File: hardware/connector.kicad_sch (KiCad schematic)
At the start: 3 parts, among them J2 2FA1-NZSP-PCBB6

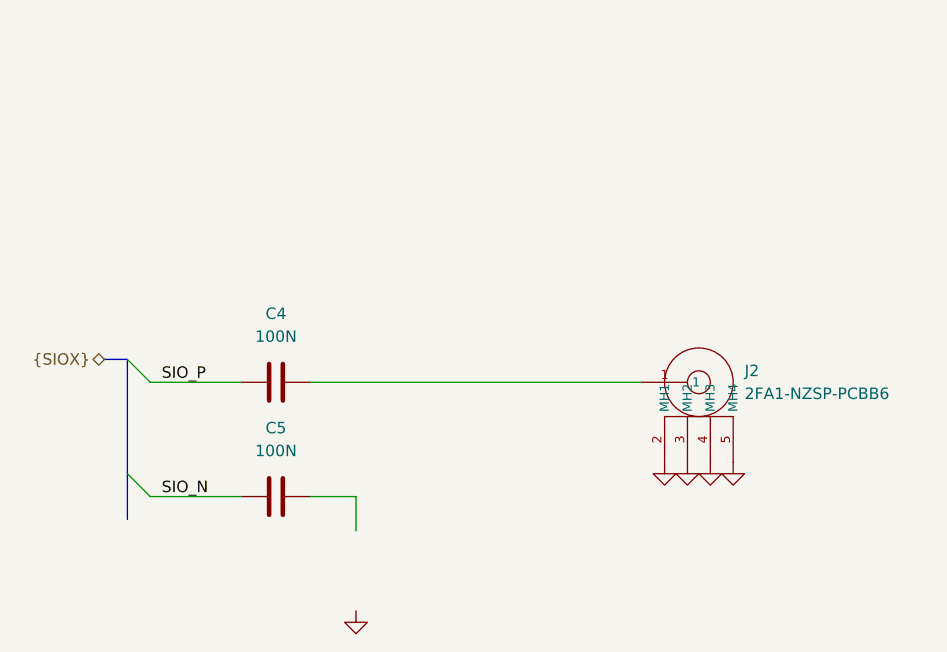
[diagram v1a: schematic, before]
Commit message: cleaned up serializer with comments and project hierarchy
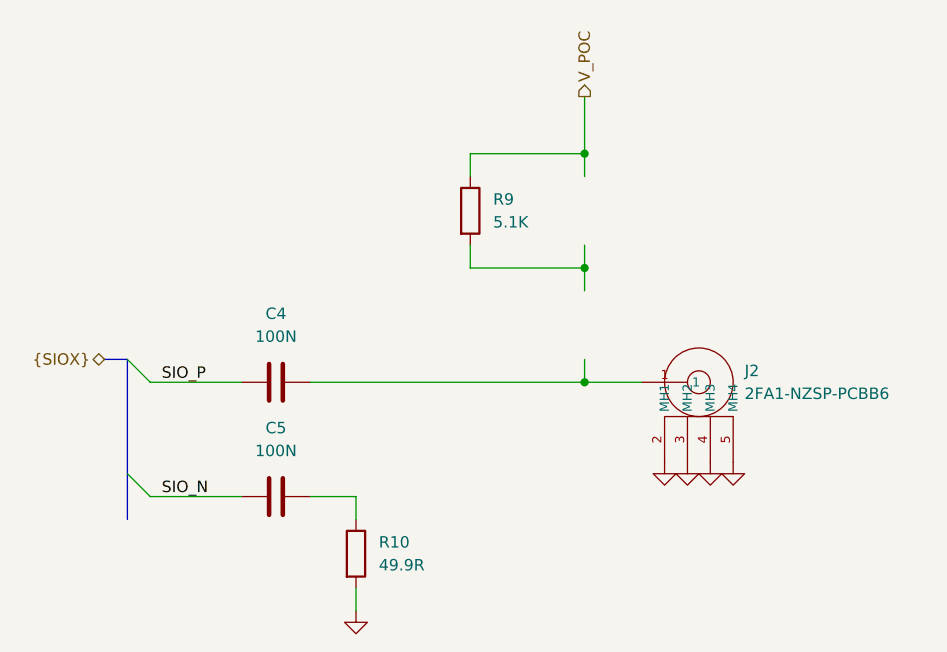
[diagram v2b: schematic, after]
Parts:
- added R10: 49.9R, Resistor_SMD:R_0402_1005Metric, symbol Device:R
- added R9: 5.1K, Resistor_SMD:R_0402_1005Metric, symbol Device:R
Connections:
- net GND: now also R10.2
- net at C5.2: now also R10.1
- new net V_POC: R9.1

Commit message: cleaned up schematics
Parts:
- added L1: PFL1005-561MRW, user:L_Coilcraft_1210POC, symbol user:1210POC-223MRC
- added L2: PFL1005-561MRW, user:L_Coilcraft_PFL1005, symbol user:PFL1005-561MRW
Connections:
- net V_POC: now also L1.1
- net at R9.2: now also L1.2, L2.1
- net at C4.2, J2.1: now also L2.2
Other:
- moved on the sheet: C4, C5, J2, R9

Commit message: started power, added smt fakra
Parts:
- removed J2: 2FA1-NZSP-PCBB6, user:2FA1-NZSP-PCBB6, symbol user:2FA1-NZSP-PCBB6
- added J2: 2FA1-NZSP-PCBB6, user:59S1AC-40MT5-Z, symbol user:59S1AC-40MT5-Z
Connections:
- net GND: now also J2.2 (MH1), J2.3 (MH2), J2.4 (MH3), J2.5 (MH4)
- net at C4.2, L2.2: now also J2.1
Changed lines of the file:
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@@
+	)
+	(symbol
+		(lib_id "user:59S1AC-40MT5-Z")
+		(at 152.4 88.9 0)
+		(unit 1)
+		(exclude_from_sim no)
+		(in_bom yes)
+		(on_board yes)
+		(dnp no)
+		(fields_autoplaced yes)
+		(property "Reference" "J2"
+			(at 157.48 87.6299 0)
+			(effects
+				(font
+					(size 1.27 1.27)
+				)
+				(justify left)
+			)
+		)
+		(property "Value" "2FA1-NZSP-PCBB6"
+			(at 157.48 90.1699 0)
+			(effects
+				(font
+					(size 1.27 1.27)
+				)
+				(justify left)
+			)
+		)
+		(property "Footprint" "user:59S1AC-40MT5-Z"
+			(at 152.4 88.9 0)
+			(effects
+				(font
+					(size 1.27 1.27)
+				)
+				(hide yes)
+			)
+		)
+		(property "Datasheet" ""
+			(at 152.4 88.9 0)
+			(effects
+				(font
+					(size 1.27 1.27)
+				)
+				(hide yes)
+			)
+		)
+		(property "Description" ""
+			(at 152.4 88.9 0)
+			(effects
+				(font
+					(size 1.27 1.27)
+				)
+				(hide yes)
+			)
+		)
+		(pin "4"
+		)
+		(pin "2"
+		)
+		(pin "5"
+		)
+		(pin "1"
+		)
+		(pin "3"
+		)
+		(instances
+			(project ""
+				(path "/d9b03904-3e0d-40cc-bc70-bbd63756773a/877d1132-b95d-4f70-9d75-8a01aff9b6a8"
+					(reference "J2")
+					(unit 1)
+				)
+			)
+		)
 	)
 	(symbol
@@
 					(unit 1)
 				)
-			)
-		)
-	)
-	(symbol
-		(lib_id "user:2FA1-NZSP-PCBB6")
-		(at 152.4 88.9 0)
-		(unit 1)
-		(exclude_from_sim no)
-		(in_bom yes)
-		(on_board yes)
-		(dnp no)
-		(fields_autoplaced yes)
-		(property "Reference" "J2"
-			(at 157.48 87.6299 0)
-			(effects
-				(font
-					(size 1.27 1.27)
-				)
-				(justify left)
-			)
-		)
-		(property "Value" "2FA1-NZSP-PCBB6"
-			(at 157.48 90.1699 0)
-			(effects
-				(font
-					(size 1.27 1.27)
-				)
-				(justify left)
-			)
-		)
-		(property "Footprint" "user:2FA1-NZSP-PCBB6"
-			(at 152.4 88.9 0)
-			(effects
-				(font
-					(size 1.27 1.27)
-				)
-				(hide yes)
-			)
-		)
-		(property "Datasheet" ""
-			(at 152.4 88.9 0)
-			(effects
-				(font
-					(size 1.27 1.27)
-				)
-				(hide yes)
-			)
-		)
-		(property "Description" ""
-			(at 152.4 88.9 0)
-			(effects
-				(font
-					(size 1.27 1.27)
-				)
-				(hide yes)
-			)
-		)
-		(pin "1"
-		)
-		(pin "3"
-		)
-		(pin "5"
-		)
-		(pin "2"
-		)
-		(pin "4"
-		)
-		(instances
-			(project "minimax"
-				(path "/d9b03904-3e0d-40cc-bc70-bbd63756773a/877d1132-b95d-4f70-9d75-8a01aff9b6a8"
-					(reference "J2")
-					(unit 1)
-				)

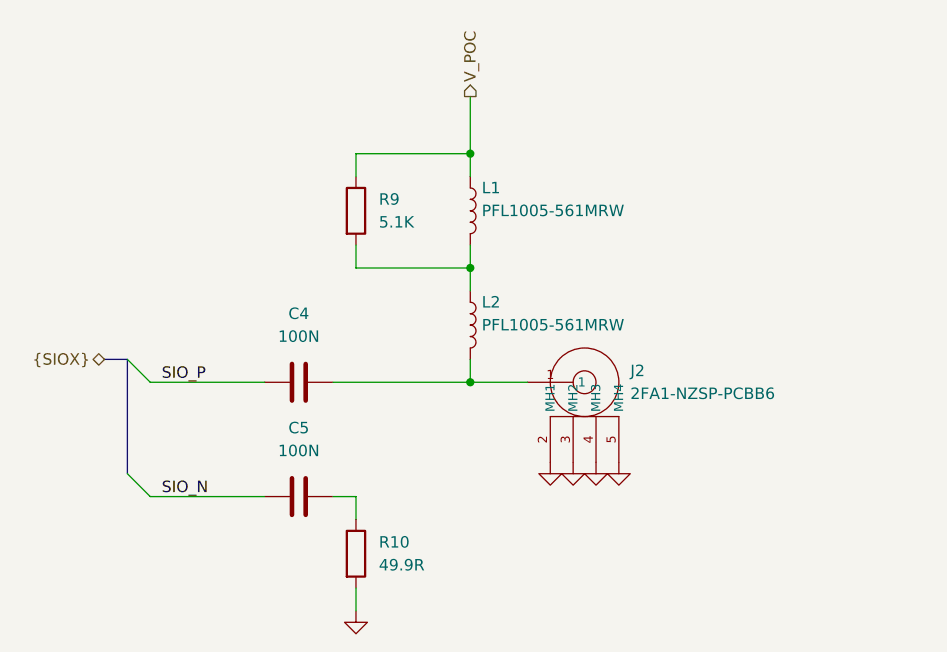
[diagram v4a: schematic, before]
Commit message: finished schematic, changed to 4 layer board
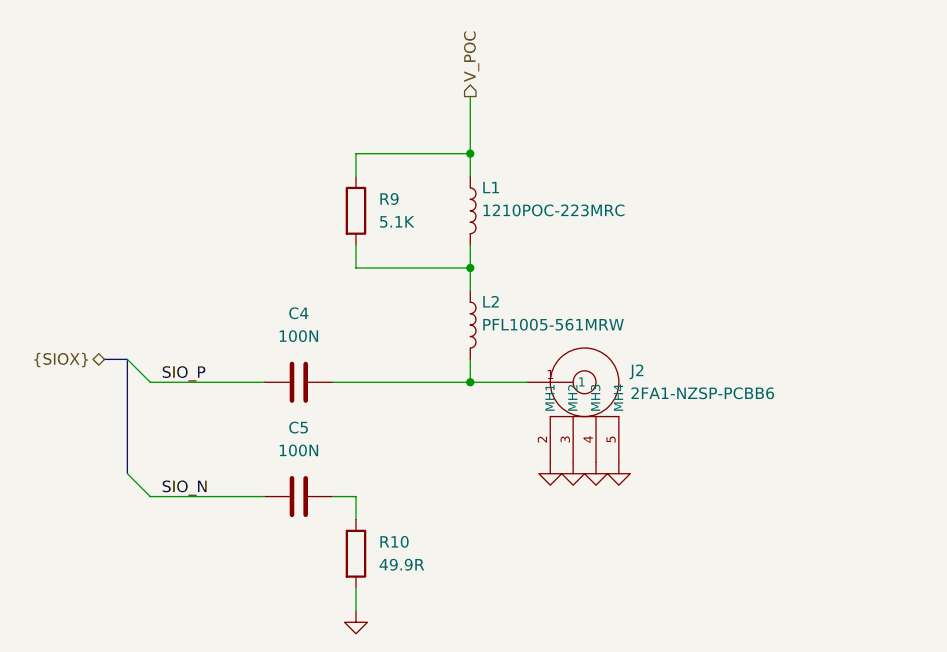
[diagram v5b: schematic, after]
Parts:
- L1: value PFL1005-561MRW -> 1210POC-223MRC
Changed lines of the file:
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@@
 			)
 		)
-		(property "Value" "PFL1005-561MRW"
+		(property "Value" "1210POC-223MRC"
 			(at 140.97 69.8499 0)
 			(effects

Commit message: layout planning and decided to use bottom layer for components
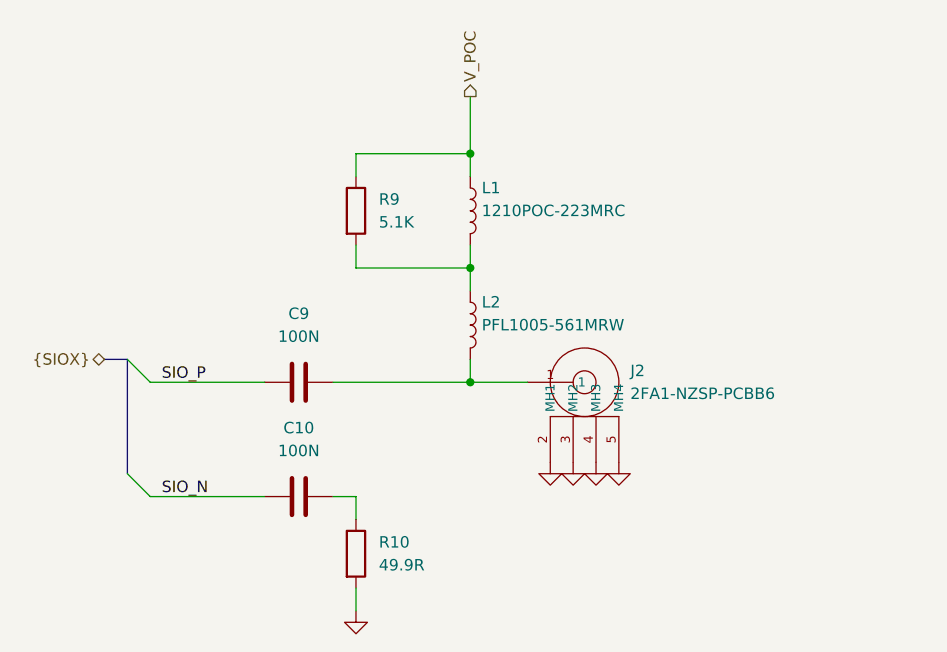
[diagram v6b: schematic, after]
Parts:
- renumbered C5 to C10, C4 to C9
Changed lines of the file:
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@@
 		(dnp no)
 		(fields_autoplaced yes)
-		(property "Reference" "#PWR010"
+		(property "Reference" "#PWR022"
 			(at 148.59 104.14 0)
 			(effects
@@
 			(project "minimax"
 				(path "/d9b03904-3e0d-40cc-bc70-bbd63756773a/877d1132-b95d-4f70-9d75-8a01aff9b6a8"
-					(reference "#PWR010")
+					(reference "#PWR022")
 					(unit 1)
 				)
@@
 		(dnp no)
 		(fields_autoplaced yes)
-		(property "Reference" "#PWR011"
+		(property "Reference" "#PWR023"
 			(at 151.13 104.14 0)
 			(effects
@@
 			(project "minimax"
 				(path "/d9b03904-3e0d-40cc-bc70-bbd63756773a/877d1132-b95d-4f70-9d75-8a01aff9b6a8"
-					(reference "#PWR011")
+					(reference "#PWR023")
 					(unit 1)
 				)
@@
 		(dnp no)
 		(fields_autoplaced yes)
-		(property "Reference" "C4"
+		(property "Reference" "C9"
 			(at 120.65 81.28 90)
 			(effects
@@
 			(project "minimax"
 				(path "/d9b03904-3e0d-40cc-bc70-bbd63756773a/877d1132-b95d-4f70-9d75-8a01aff9b6a8"
-					(reference "C4")
+					(reference "C9")
 					(unit 1)
 				)
@@
 		(dnp no)
 		(fields_autoplaced yes)
-		(property "Reference" "#PWR014"
+		(property "Reference" "#PWR026"
 			(at 127 120.65 0)
 			(effects
@@
 			(project "minimax"
 				(path "/d9b03904-3e0d-40cc-bc70-bbd63756773a/877d1132-b95d-4f70-9d75-8a01aff9b6a8"
-					(reference "#PWR014")
+					(reference "#PWR026")
 					(unit 1)
 				)
@@
 		(dnp no)
 		(fields_autoplaced yes)
-		(property "Reference" "C5"
+		(property "Reference" "C10"
 			(at 120.65 93.98 90)
 			(effects
@@
 			(project "minimax"
 				(path "/d9b03904-3e0d-40cc-bc70-bbd63756773a/877d1132-b95d-4f70-9d75-8a01aff9b6a8"
-					(reference "C5")
+					(reference "C10")
 					(unit 1)
 				)
@@
 		(dnp no)
 		(fields_autoplaced yes)
-		(property "Reference" "#PWR012"
+		(property "Reference" "#PWR024"
 			(at 153.67 104.14 0)
 			(effects
@@
 			(project "minimax"
 				(path "/d9b03904-3e0d-40cc-bc70-bbd63756773a/877d1132-b95d-4f70-9d75-8a01aff9b6a8"
-					(reference "#PWR012")
+					(reference "#PWR024")
 					(unit 1)
 				)
@@
 		(dnp no)
 		(fields_autoplaced yes)
-		(property "Reference" "#PWR013"
+		(property "Reference" "#PWR025"
 			(at 156.21 104.14 0)
 			(effects
@@
 			(project "minimax"
 				(path "/d9b03904-3e0d-40cc-bc70-bbd63756773a/877d1132-b95d-4f70-9d75-8a01aff9b6a8"
-					(reference "#PWR013")
-					(unit 1)
-				)
+					(reference "#PWR025")
+					(unit 1)
+				)

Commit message: clean up
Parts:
- J2: value 2FA1-NZSP-PCBB6 -> 59S1AC-40MT5-Z
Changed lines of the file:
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@@
 			)
 		)
-		(property "Value" "2FA1-NZSP-PCBB6"
+		(property "Value" "59S1AC-40MT5-Z"
 			(at 157.48 90.1699 0)
 			(effects

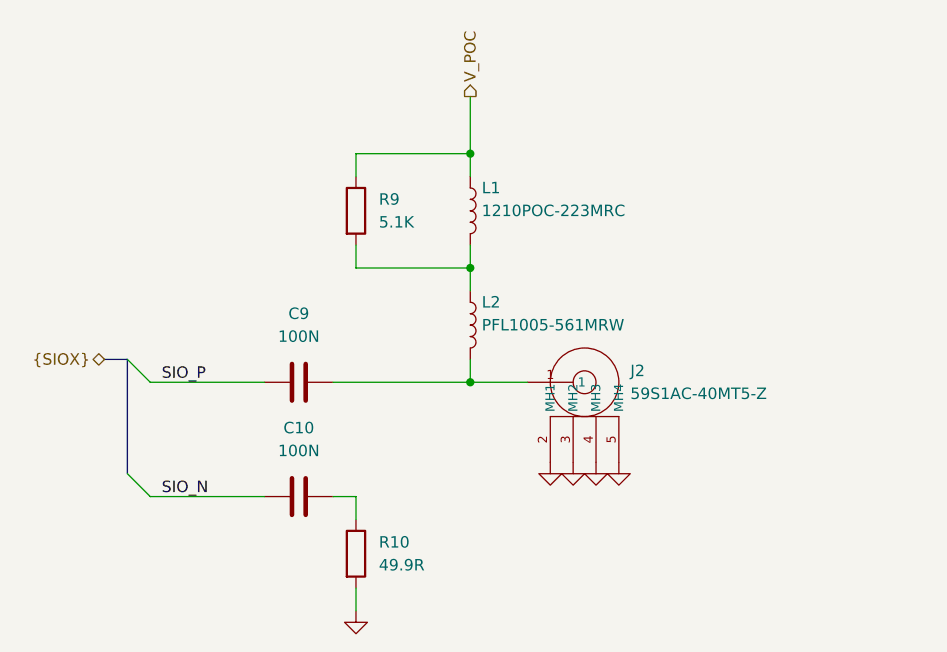
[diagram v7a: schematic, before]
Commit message: added LED circuits and test points on extra MFPs
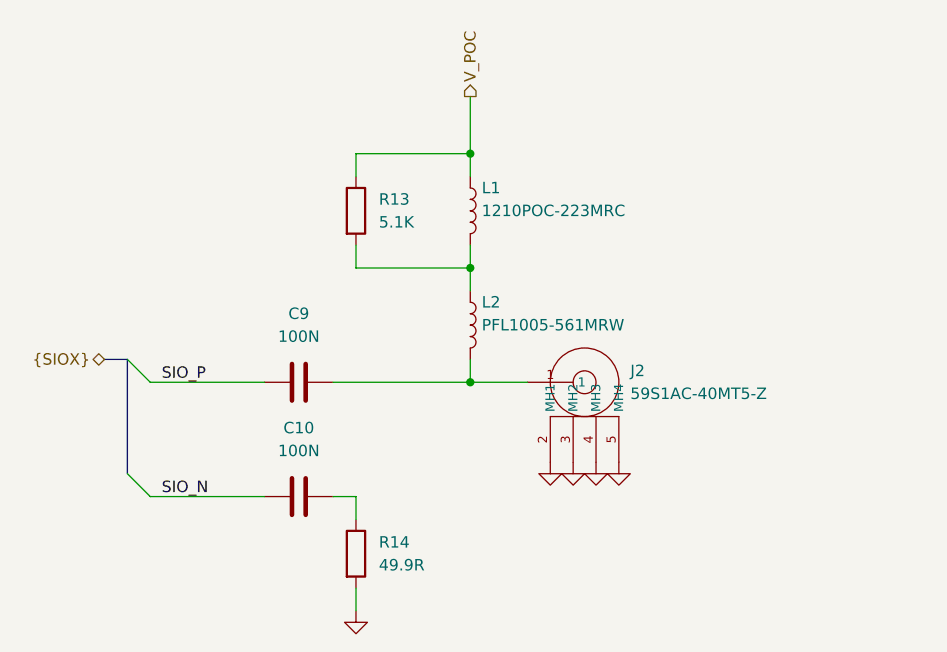
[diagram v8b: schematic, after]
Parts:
- renumbered R9 to R13, R10 to R14
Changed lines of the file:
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@@
 		(dnp no)
 		(fields_autoplaced yes)
-		(property "Reference" "R9"
+		(property "Reference" "R13"
 			(at 129.54 68.5799 0)
 			(effects
@@
 			(project "minimax"
 				(path "/d9b03904-3e0d-40cc-bc70-bbd63756773a/877d1132-b95d-4f70-9d75-8a01aff9b6a8"
-					(reference "R9")
+					(reference "R13")
 					(unit 1)
 				)
@@
 		(dnp no)
 		(fields_autoplaced yes)
-		(property "Reference" "#PWR022"
+		(property "Reference" "#PWR030"
 			(at 148.59 104.14 0)
 			(effects
@@
 			(project "minimax"
 				(path "/d9b03904-3e0d-40cc-bc70-bbd63756773a/877d1132-b95d-4f70-9d75-8a01aff9b6a8"
-					(reference "#PWR022")
+					(reference "#PWR030")
 					(unit 1)
 				)
@@
 		(dnp no)
 		(fields_autoplaced yes)
-		(property "Reference" "#PWR023"
+		(property "Reference" "#PWR031"
 			(at 151.13 104.14 0)
 			(effects
@@
 			(project "minimax"
 				(path "/d9b03904-3e0d-40cc-bc70-bbd63756773a/877d1132-b95d-4f70-9d75-8a01aff9b6a8"
-					(reference "#PWR023")
+					(reference "#PWR031")
 					(unit 1)
 				)
@@
 		(dnp no)
 		(fields_autoplaced yes)
-		(property "Reference" "#PWR026"
+		(property "Reference" "#PWR034"
 			(at 127 120.65 0)
 			(effects
@@
 			(project "minimax"
 				(path "/d9b03904-3e0d-40cc-bc70-bbd63756773a/877d1132-b95d-4f70-9d75-8a01aff9b6a8"
-					(reference "#PWR026")
+					(reference "#PWR034")
 					(unit 1)
 				)
@@
 		(dnp no)
 		(fields_autoplaced yes)
-		(property "Reference" "#PWR024"
+		(property "Reference" "#PWR032"
 			(at 153.67 104.14 0)
 			(effects
@@
 			(project "minimax"
 				(path "/d9b03904-3e0d-40cc-bc70-bbd63756773a/877d1132-b95d-4f70-9d75-8a01aff9b6a8"
-					(reference "#PWR024")
+					(reference "#PWR032")
 					(unit 1)
 				)
@@
 		(dnp no)
 		(fields_autoplaced yes)
-		(property "Reference" "R10"
+		(property "Reference" "R14"
 			(at 129.54 106.6799 0)
 			(effects
@@
 			(project "minimax"
 				(path "/d9b03904-3e0d-40cc-bc70-bbd63756773a/877d1132-b95d-4f70-9d75-8a01aff9b6a8"
-					(reference "R10")
+					(reference "R14")
 					(unit 1)
 				)
@@
 		(dnp no)
 		(fields_autoplaced yes)
-		(property "Reference" "#PWR025"
+		(property "Reference" "#PWR033"
 			(at 156.21 104.14 0)
 			(effects
@@
 			(project "minimax"
 				(path "/d9b03904-3e0d-40cc-bc70-bbd63756773a/877d1132-b95d-4f70-9d75-8a01aff9b6a8"
-					(reference "#PWR025")
-					(unit 1)
-				)
+					(reference "#PWR033")
+					(unit 1)
+				)
